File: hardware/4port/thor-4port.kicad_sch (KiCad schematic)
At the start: 17 parts, among them J1 THOR J47 / Wieson, J10 AUX / RAW IO, J12 SHIELD / GND / OPEN, J2 FSI_CAN0 / CAN, J3 FSI_CAN1 / CAN, J4 AURIX_CAN1 / CAN, J5 AURIX_CAN2 / CAN

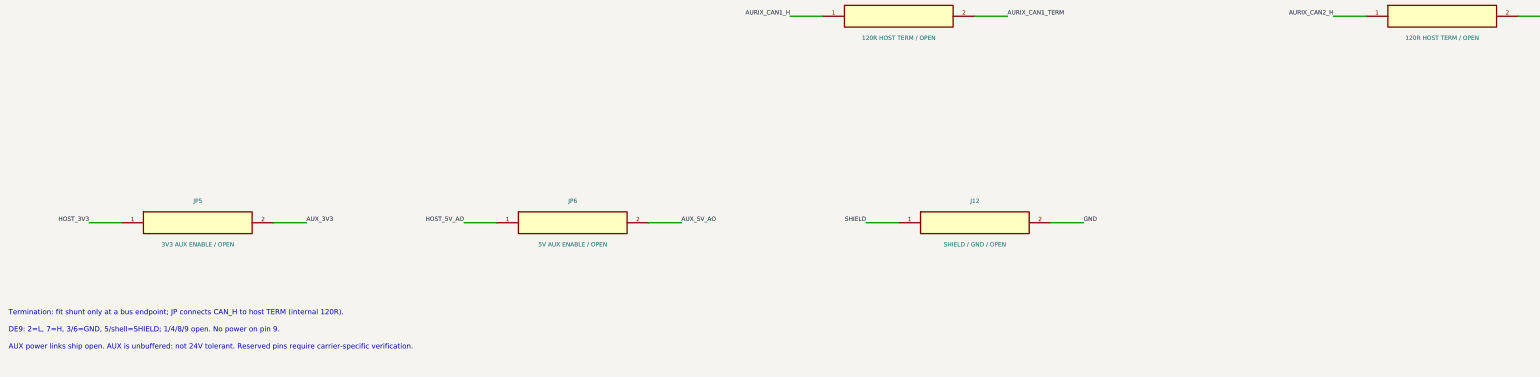
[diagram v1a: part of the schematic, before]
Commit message: Add prototype access, clear controls and reinforced mounting housings
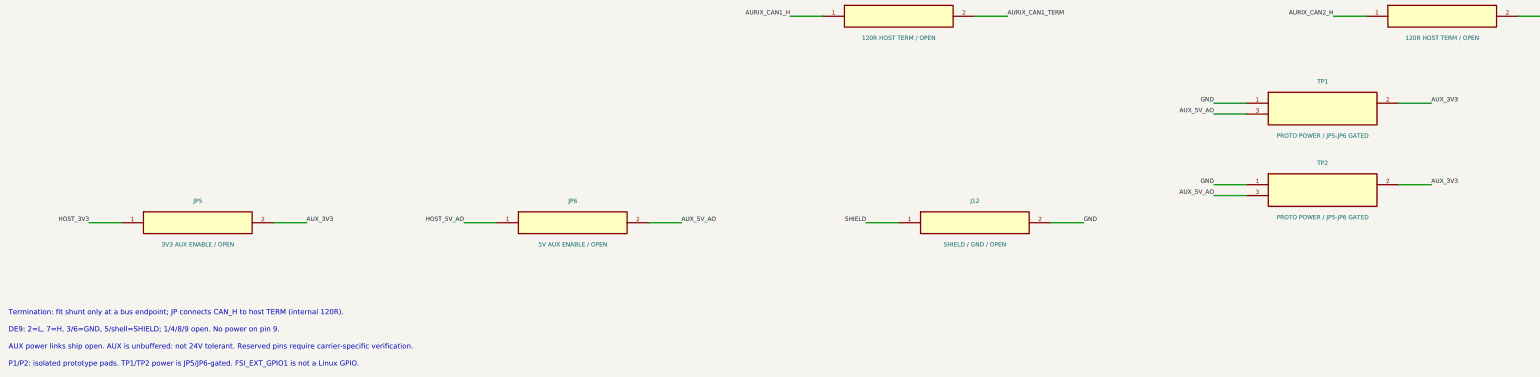
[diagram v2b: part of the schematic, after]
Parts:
- added TP1: PROTO POWER / JP5-JP6 GATED, Thor:Prototype_Power_3x3_P2.54, symbol Thor:TP1_function
- added TP2: PROTO POWER / JP5-JP6 GATED, Thor:Prototype_Power_3x3_P2.54, symbol Thor:TP2_function
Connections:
- net AUX_3V3: now also TP1.2 (AUX_3V3), TP2.2 (AUX_3V3)
- net AUX_5V_AO: now also TP1.3 (AUX_5V_AO), TP2.3 (AUX_5V_AO)
- net GND: now also TP1.1 (GND), TP2.1 (GND)
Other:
- note added: "P1/P2: isolated prototype pads. TP1/TP2 power is JP5/JP6-gated. FSI_EXT_GPIO1 is not a Linux GPIO."
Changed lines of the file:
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@@
 (wire(pts(xy 261.62 248.92)(xy 269.24 248.92))(stroke(width 0)(type default)))
 (label "GND"(at 269.24 248.92 0)(effects(font(size 1 1))(justify left bottom)))
+(symbol(lib_id "Thor:TP1_function")(at 325.12 222.25 0)(unit 1)(in_bom no)(on_board yes)(dnp no)
+(property "Reference" "TP1"(at 325.12 215.9 0)(effects(font(size 1 1))))
+(property "Value" "PROTO POWER / JP5-JP6 GATED"(at 325.12 228.6 0)(effects(font(size 1 1))))
+(property "Footprint" "Thor:Prototype_Power_3x3_P2.54"(at 325.12 222.25 0)(effects(font(size 1 1))(hide yes)))
+(property "MPN" ""(at 325.12 222.25 0)(effects(font(size 1 1))(hide yes)))
+(property "LCSC" ""(at 325.12 222.25 0)(effects(font(size 1 1))(hide yes)))
+(pin "1")
+(pin "2")
+(pin "3")
+(instances(project "thor-4port"(path "/7344a2f4-8aa6-51e2-a58b-a8d2edd9d164"(reference "TP1")(unit 1)))))
+(wire(pts(xy 307.34000000000003 220.98)(xy 299.72 220.98))(stroke(width 0)(type default)))
+(label "GND"(at 299.72 220.98 0)(effects(font(size 1 1))(justify right bottom)))
+(wire(pts(xy 342.9 220.98)(xy 350.52 220.98))(stroke(width 0)(type default)))
+(label "AUX_3V3"(at 350.52 220.98 0)(effects(font(size 1 1))(justify left bottom)))
+(wire(pts(xy 307.34000000000003 223.52)(xy 299.72 223.52))(stroke(width 0)(type default)))
+(label "AUX_5V_AO"(at 299.72 223.52 0)(effects(font(size 1 1))(justify right bottom)))
+(symbol(lib_id "Thor:TP2_function")(at 325.12 241.3 0)(unit 1)(in_bom no)(on_board yes)(dnp no)
+(property "Reference" "TP2"(at 325.12 234.95000000000002 0)(effects(font(size 1 1))))
+(property "Value" "PROTO POWER / JP5-JP6 GATED"(at 325.12 247.65 0)(effects(font(size 1 1))))
+(property "Footprint" "Thor:Prototype_Power_3x3_P2.54"(at 325.12 241.3 0)(effects(font(size 1 1))(hide yes)))
+(property "MPN" ""(at 325.12 241.3 0)(effects(font(size 1 1))(hide yes)))
+(property "LCSC" ""(at 325.12 241.3 0)(effects(font(size 1 1))(hide yes)))
+(pin "1")
+(pin "2")
+(pin "3")
+(instances(project "thor-4port"(path "/7344a2f4-8aa6-51e2-a58b-a8d2edd9d164"(reference "TP2")(unit 1)))))
+(wire(pts(xy 307.34000000000003 240.03)(xy 299.72 240.03))(stroke(width 0)(type default)))
+(label "GND"(at 299.72 240.03 0)(effects(font(size 1 1))(justify right bottom)))
+(wire(pts(xy 342.9 240.03)(xy 350.52 240.03))(stroke(width 0)(type default)))
+(label "AUX_3V3"(at 350.52 240.03 0)(effects(font(size 1 1))(justify left bottom)))
+(wire(pts(xy 307.34000000000003 242.57000000000002)(xy 299.72 242.57000000000002))(stroke(width 0)(type default)))
+(label "AUX_5V_AO"(at 299.72 242.57000000000002 0)(effects(font(size 1 1))(justify right bottom)))
 (text "Termination: fit shunt only at a bus endpoint; JP connects CAN_H to host TERM (internal 120R)."(at 18 270 0)(effects(font(size 1.2 1.2))(justify left)))
 (text "DE9: 2=L, 7=H, 3/6=GND, 5/shell=SHIELD; 1/4/8/9 open. No power on pin 9."(at 18 274 0)(effects(font(size 1.2 1.2))(justify left)))
 (text "AUX power links ship open. AUX is unbuffered: not 24V tolerant. Reserved pins require carrier-specific verification."(at 18 278 0)(effects(font(size 1.2 1.2))(justify left)))
+(text "P1/P2: isolated prototype pads. TP1/TP2 power is JP5/JP6-gated. FSI_EXT_GPIO1 is not a Linux GPIO."(at 18 282 0)(effects(font(size 1.2 1.2))(justify left)))
 )
